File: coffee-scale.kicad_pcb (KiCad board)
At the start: 2 copper layers, 62 x 42 mm, 36 parts, among them IC1 esp8266-07, IC2 HX711, J1 Conn_01x04, J3 Conn_01x05_Male, J4 Conn_01x01_Male, J5 Conn_01x02, Q1 MMBT3906, SW1 SW_Push_JTP-1130, U1 LM1117-3.3

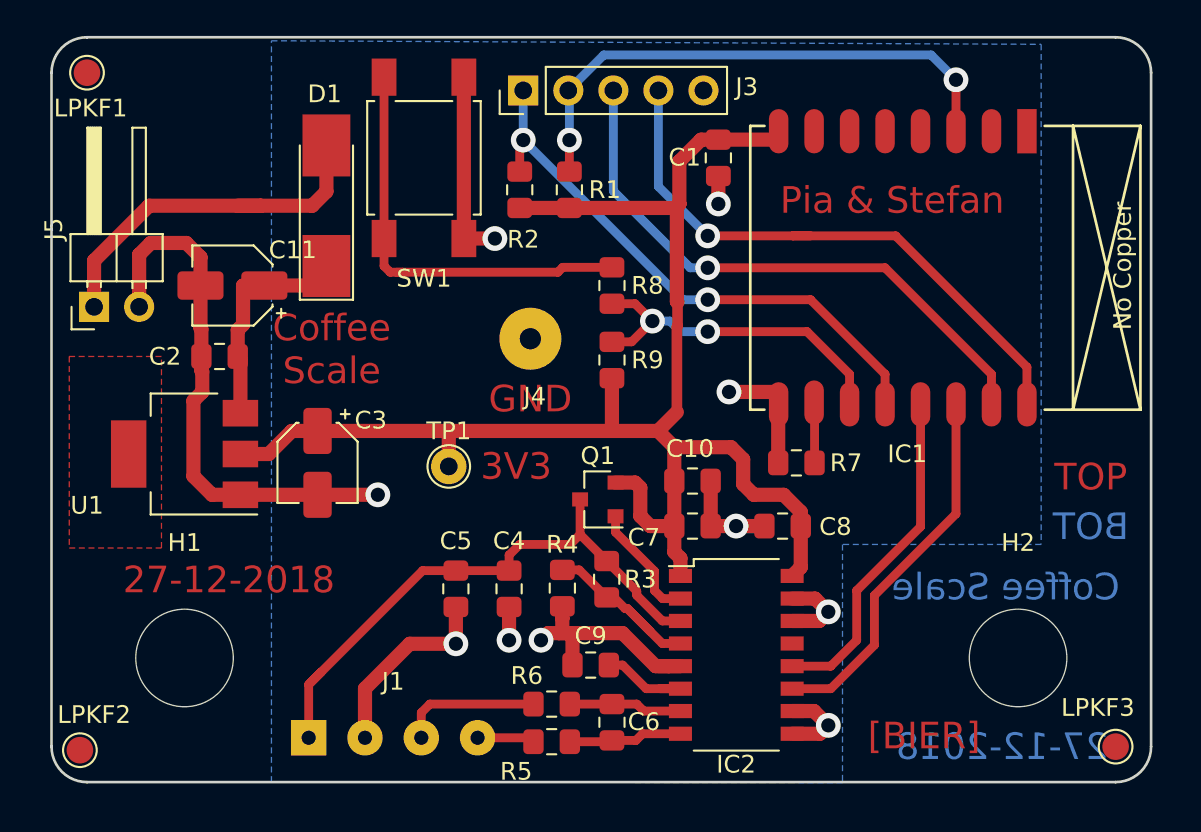
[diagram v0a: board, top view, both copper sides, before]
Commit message: next pcb version
fix esp position
add descriptions to copper
fix hole positions

Signed-off-by: Stefan Guelland <sguelland@thinkpad.za.w-hs.de>
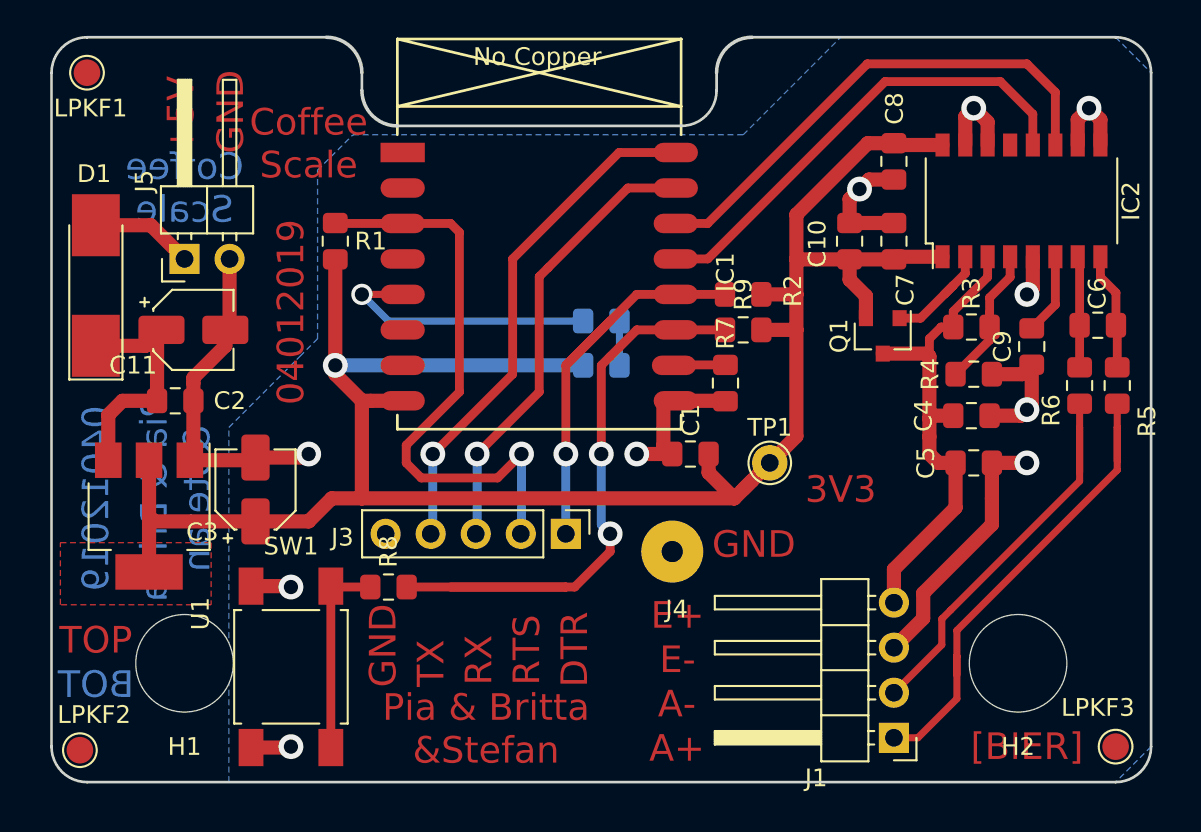
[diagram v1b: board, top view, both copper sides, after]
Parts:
- added D2: LW_M673, Library:LW_M673, B.Cu at (109.5, 121.0)
- added R10: 250, Resistor_SMD:R_0805_2012Metric_Pad1.15x1.40mm_HandSolder, B.Cu at (109.5, 123.5)
- C10, C5: value 10u -> 1u
- J1: footprint Connector_Wire:SolderWirePad_1x04_P3.175mm_Drill0.8mm -> Connector_PinHeader_2.54mm:PinHeader_1x04_P2.54mm_Horizontal
- moved R6 37.7 mm to (138.6, 124.6), turned to 90 degrees
- moved C6 35.4 mm to (137.5, 121.2), turned to 0 degrees
- moved R5 34.8 mm to (136.5, 124.6), turned to 270 degrees
- moved IC1 34.5 mm to (99.0, 111.5), turned to 0 degrees
- moved J1 33.0 mm to (126.0, 144.5), turned to 180 degrees
- moved C9 30.7 mm to (133.8, 122.4), turned to 90 degrees
- moved IC2 30.2 mm to (133.2, 114.2), turned to 90 degrees
- moved C5 30.1 mm to (130.5, 129.0), turned to 0 degrees
- moved SW1 29.7 mm to (92.0, 140.5), turned to 90 degrees
- moved C4 27.8 mm to (130.4, 126.3), turned to 0 degrees
- moved R4 26.1 mm to (130.5, 124.0), turned to 0 degrees
- moved J3 25.1 mm to (107.5, 133.0), turned to 270 degrees
- moved R3 25.0 mm to (130.4, 121.3), turned to 0 degrees
- moved C8 21.5 mm to (126.0, 112.0), turned to 270 degrees
- moved R8 21.2 mm to (97.5, 136.0), turned to 180 degrees
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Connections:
- C4 pad 1: Net-(C4-Pad1) -> /E+
- C5 pad 1: Net-(C4-Pad1) -> /E+
- IC1 pad 5: Net-(IC1-Pad5) -> LED
- IC2 pad 3: Net-(C4-Pad1) -> /E+
- J1 pad 1: Net-(C4-Pad1) -> /A+
- J1 pad 2: GND -> /A-
- J1 pad 3: Net-(J1-Pad3) -> GND
- J1 pad 4: Net-(J1-Pad4) -> /E+
- Q1 pad 3: Net-(C4-Pad1) -> /E+
- R3 pad 1: Net-(C4-Pad1) -> /E+
- R5 pad 2: Net-(J1-Pad3) -> /A-
- R6 pad 1: Net-(J1-Pad4) -> /A+
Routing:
- net Net-(C4-Pad1): track 33.0 -> 0.00 mm
- net +3V3: track 87.5 -> 118.3 mm, vias 0 -> 1
- net /E+: track 0.00 -> 28.0 mm
- net /A+: track 0.00 -> 27.8 mm
- net /A-: track 0.00 -> 23.2 mm
- net GND: track 91.9 -> 72.9 mm
- net Button: track 18.8 -> 37.3 mm
- net LED: track 0.00 -> 16.1 mm, vias 0 -> 1
- net /5V_IN: track 21.2 -> 5.79 mm
- net Net-(R8-Pad2): track 24.1 -> 11.3 mm
- net Net-(J1-Pad3): track 7.94 -> 0.00 mm
- net HX711_DOUT: track 19.7 -> 27.5 mm
- net HX711_SCK: track 21.8 -> 29.5 mm
- net ~Bootloader: track 31.5 -> 24.1 mm, vias 2 -> 1
- net RXD0: track 32.3 -> 25.2 mm
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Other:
- outline, holes or cut-outs redrawn
- board text added: "+5V"
- board text added: "04012019"
- board text added: "A+"
- board text added: "A-"
- board text added: "DTR"
- board text added: "E+"
- board text added: "E-"
- board text added: "Pia & Britta &Stefan"
- board text added: "RTS"
- board text added: "RX"
- board text added: "TX"
- board text removed: "27-12-2018"
- board text removed: "Pia & Stefan"
